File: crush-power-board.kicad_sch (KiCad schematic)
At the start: 8 parts

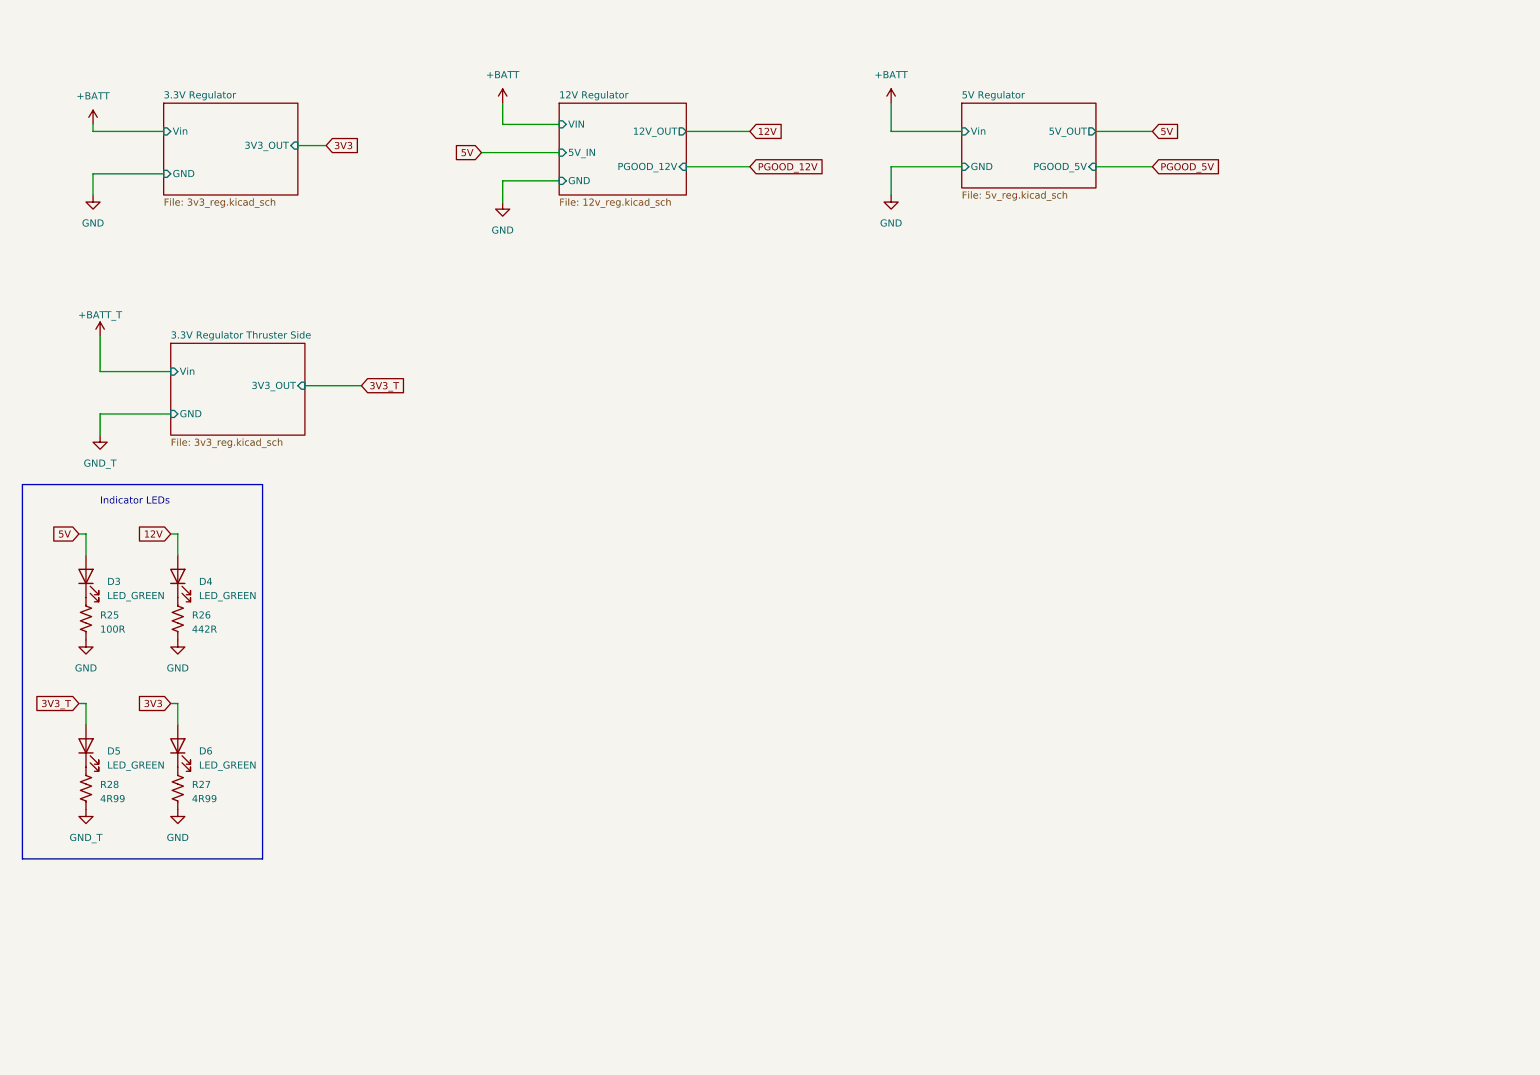
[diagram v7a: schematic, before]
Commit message: Added connections to signal board, battery, and mounting holes
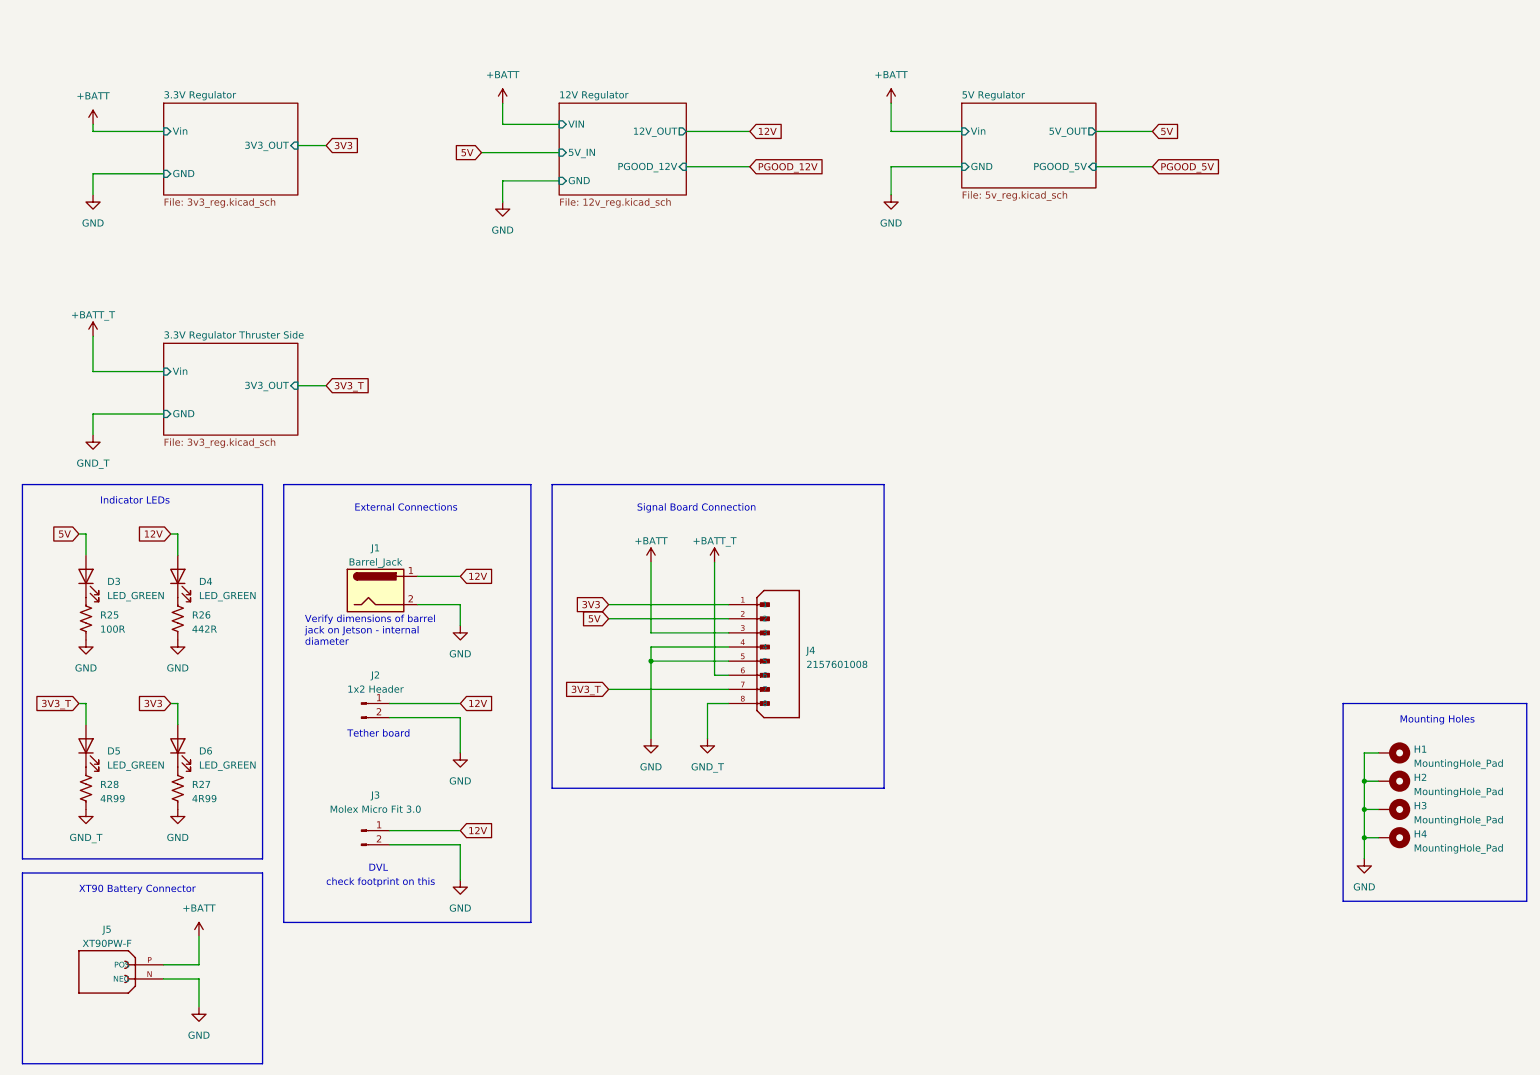
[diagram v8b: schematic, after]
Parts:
- added H1, H2, H3, H4: MountingHole_Pad, symbol Mechanical:MountingHole_Pad
- added J1: Barrel_Jack, Connector_BarrelJack:BarrelJack_Horizontal, symbol Connector:Barrel_Jack
- added J2: 1x2 Header, Connector_PinHeader_2.54mm:PinHeader_1x02_P2.54mm_Horizontal, symbol Connector:Conn_01x02_Pin
- added J3: Molex Micro Fit 3.0, Connector_Molex:Molex_Micro-Fit_3.0_43045-0212_2x01_P3.00mm_Vertical, symbol Connector:Conn_01x02_Pin
- added J4: 2157601008, crush-power-footprints:MOLEX_2157601008, symbol crush-power-lib:2157601008
- added J5: XT90PW-F, crush-power-footprints:AMASS_XT90PW-F, symbol crush-power-lib:XT90PW-F
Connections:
- net +BATT: now also J4.3, J4.6, J5.P (POS)
- net 12V: now also J1.1, J2.1 (Pin_1), J3.1 (Pin_1)
- net 3V3: now also J4.1
- net 3V3_T: now also J4.7
- net 5V: now also J4.2
- net GND: now also H1.1, H2.1, H3.1, H4.1, J1.2, J2.2 (Pin_2), J3.2 (Pin_2), J4.4, J4.5, J4.8, J5.N (NEG)
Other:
- note added: "DVL"
- note added: "External Connections"
- note added: "Mounting Holes"
- note added: "Signal Board Connection"
- note added: "Tether board"
- note added: "Verify dimensions of barrel jack on Jetson - internal diameter"
- note added: "XT90 Battery Connector"
- note added: "check footprint on this"
